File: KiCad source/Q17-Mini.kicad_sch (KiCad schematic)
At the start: 80 parts, among them J1 Input, J2-1 SPK+, J2-2 SPK-, J3-1 V+, J3-2 GND, J3-3 V-, Q1 IRF610, Q10 KSA992, Q11 ZVP2106A, Q12 BD139, Q13 IRF610, Q14 IRF9610, Q15 FQA46N15, Q16 FQA36P15, Q2 KSA992, Q3 KSC1845, Q4 IRF9610, Q5 FQP3P20, Q6 FQP3N30, Q7 KSC1845, Q8 ZVN4206AV, Q9 ZVP2106A, U1 OPA1641

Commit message: Update Q17-Mini.kicad_sch
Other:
- note added: "0.25W, 0.5W resistor : Vishay CCF07 or MRS25"
- note added: "1W resistor : Vishay PR01"
- note added: "2W resistor : Vishay CCF02 or PR02"
- note added: "C13, C14 : Panasonic FC"
- note added: "C3, C5 : ELna Silmic II 100uF 16v"
- note added: "max 55V"
- note removed: "0.5W, 1W resistor : Vishay PR01"
- note removed: "2W resistor : Vishay CCF or PR02"
- note removed: "C3, C5, C13, C14 : Panasonic FC"
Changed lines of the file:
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@@
     (title "Q17-Mini Amplifier")
     (date "2021-12-22")
-    (rev "1.1.7")
+    (rev "1.1.8")
     (company "by eng. Tiberiu Vicol")
     (comment 1 "Modified by Stef for the Q17-Mini project")
@@
     (stroke (width 0) (type solid) (color 0 0 0 0))
   )
-  (text "C3, C5, C13, C14 : Panasonic FC " (at 60.96 170.18 0)
-    (effects (font (size 1.27 1.27)) (justify left bottom))
-  )
-  (text "0.5W, 1W resistor : Vishay PR01" (at 60.96 177.8 0)
+  (text "C3, C5 : ELna Silmic II 100uF 16v" (at 59.69 173.99 0)
+    (effects (font (size 1.27 1.27)) (justify left bottom))
+  )
+  (text "max 55V" (at 266.7 71.12 0)
+    (effects (font (size 1.27 1.27)) (justify left bottom))
+  )
+  (text "1W resistor : Vishay PR01" (at 59.69 177.8 0)
     (effects (font (size 1.27 1.27)) (justify left bottom))
   )
   (text "C1, C10 : use Mica CDE CD15 or Polystyrene capacitor."
-    (at 95.25 193.04 0)
+    (at 96.52 193.04 0)
     (effects (font (size 1.27 1.27)) (justify left bottom))
   )
   (text "J2 and J3: FASTON 250 PCB connector (TE Connectivity 63849-1)"
-    (at 95.25 196.85 0)
+    (at 96.52 196.85 0)
     (effects (font (size 1.27 1.27)) (justify left bottom))
   )
@@
   )
   (text "C7 : use MKP capacitor (MKP1F041005I00JYSD or MKP4D041005D00JSSD)."
-    (at 95.25 181.61 0)
-    (effects (font (size 1.27 1.27)) (justify left bottom))
-  )
-  (text "D2, D3 : 1N5248B" (at 60.96 193.04 0)
-    (effects (font (size 1.27 1.27)) (justify left bottom))
-  )
-  (text "2W resistor : Vishay CCF or PR02" (at 60.96 181.61 0)
+    (at 96.52 181.61 0)
+    (effects (font (size 1.27 1.27)) (justify left bottom))
+  )
+  (text "D2, D3 : 1N5248B" (at 59.69 193.04 0)
+    (effects (font (size 1.27 1.27)) (justify left bottom))
+  )
+  (text "2W resistor : Vishay CCF02 or PR02" (at 59.69 181.61 0)
     (effects (font (size 1.27 1.27)) (justify left bottom))
   )
@@
   )
   (text "R26, R27, R28 : try to use non inductive 1W resistor (Vishay Dale or Ohmite)."
-    (at 95.25 173.99 0)
-    (effects (font (size 1.27 1.27)) (justify left bottom))
-  )
-  (text "D1, D4 : LED RED 2V" (at 60.96 189.23 0)
+    (at 96.52 173.99 0)
+    (effects (font (size 1.27 1.27)) (justify left bottom))
+  )
+  (text "D1, D4 : LED RED 2V" (at 59.69 189.23 0)
     (effects (font (size 1.27 1.27)) (justify left bottom))
   )
@@
   )
   (text "C15, C16 : Vishay 048 RML (MAL204858222E3) or Nichicon UFW (UFW1J222MHD)."
-    (at 95.25 177.8 0)
+    (at 96.52 177.8 0)
     (effects (font (size 1.27 1.27)) (justify left bottom))
   )
@@
   )
   (text "C2 : use bipolar capacitor (Nichicon Muse UES1A101MPM)."
-    (at 95.25 189.23 0)
+    (at 96.52 189.23 0)
+    (effects (font (size 1.27 1.27)) (justify left bottom))
+  )
+  (text "0.25W, 0.5W resistor : Vishay CCF07 or MRS25" (at 96.52 170.18 0)
     (effects (font (size 1.27 1.27)) (justify left bottom))
   )
@@
     (effects (font (size 1.27 1.27)) (justify left bottom))
   )
+  (text "C13, C14 : Panasonic FC " (at 59.69 185.42 0)
+    (effects (font (size 1.27 1.27)) (justify left bottom))
+  )
   (text "Q15 : FQA46N15" (at 13.97 193.04 0)
     (effects (font (size 1.27 1.27)) (justify left bottom))
@@
     (effects (font (size 1.27 1.27)) (justify left bottom))
   )
-  (text "POWER 48VDC" (at 266.7 71.12 0)
+  (text "POWER 48VDC" (at 266.7 68.58 0)
     (effects (font (size 1.27 1.27)) (justify left bottom))
   )
   (text "C17 : use MKP capacitor (MKP1F031004B00KI00 or FKP3C031004C00JSSD)."
-    (at 95.25 185.42 0)
+    (at 96.52 185.42 0)
     (effects (font (size 1.27 1.27)) (justify left bottom))
   )
@@
     (effects (font (size 1.27 1.27)) (justify left bottom))
   )
-  (text "U1 : OPA1641 or OPA1611" (at 60.96 185.42 0)
-    (effects (font (size 1.27 1.27)) (justify left bottom))
-  )
-  (text "D5, D6 : 1N5245" (at 60.96 196.85 0)
-    (effects (font (size 1.27 1.27)) (justify left bottom))
-  )
-  (text "Do not power on the board without opamp." (at 240.03 15.24 0)
-    (effects (font (size 1.27 1.27) (thickness 0.254) bold) (justify left bottom))
-  )
-  (text "100nF capacitor : Wima MKS2" (at 60.96 173.99 0)
-    (effects (font (size 1.27 1.27)) (justify left bottom))
-  )
+  (text "U1 : OPA1641 or OPA1611" (at 13.97 154.94 0)
+    (effects (font (size 1.27 1.27)) (justify left bottom))
+  )
+  (text "D5, D6 : 1N5245" (at 59.69 196.85 0)
+    (effects (font (size 1.27 1.27)) (justify left bottom))
+  )
+  (text "Do not power on the board without opamp." (at 233.68 15.24 0)
+    (effects (font (size 1.5 1.5) (thickness 0.254) bold) (justify left bottom))
+  )
+  (text "100nF capacitor : Wima MKS2" (at 59.69 170.18 0)
+    (effects (font (size 1.27 1.27)) (justify left bottom))
+  )

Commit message: Update diagrams
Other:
- note added: "DC Fuse : 3A Fast"
- note added: "POWER 45VDC"
- note removed: "DC Fuse : 3A"
- note removed: "POWER 48VDC"
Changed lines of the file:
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@@
   (title_block
     (title "Q17-Mini Amplifier")
-    (date "2021-12-22")
+    (date "2021-12-23")
     (rev "1.1.8")
     (company "by eng. Tiberiu Vicol")
@@
     (effects (font (size 1.27 1.27) (thickness 0.254) bold) (justify left bottom))
   )
-  (text "DC Fuse : 3A" (at 266.7 96.52 0)
+  (text "DC Fuse : 3A Fast" (at 264.16 96.52 0)
     (effects (font (size 1.27 1.27)) (justify left bottom))
   )
@@
     (effects (font (size 1.27 1.27)) (justify left bottom))
   )
-  (text "POWER 48VDC" (at 266.7 68.58 0)
-    (effects (font (size 1.27 1.27)) (justify left bottom))
-  )
+  (text "POWER 45VDC" (at 266.7 68.58 0)
+    (effects (font (size 1.27 1.27)) (justify left bottom))
+  )

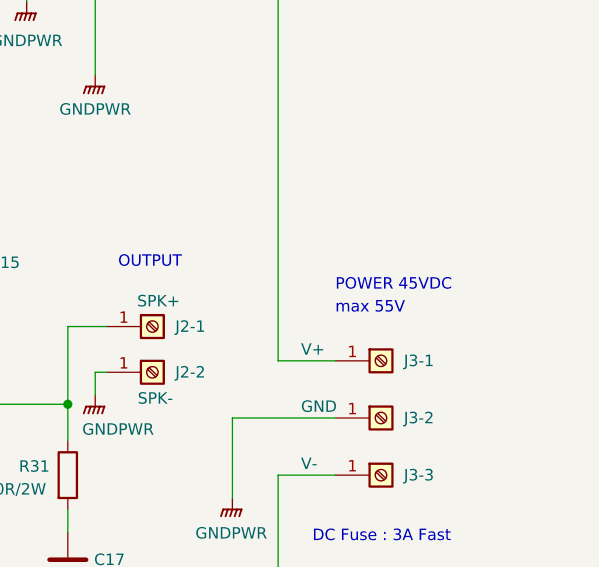
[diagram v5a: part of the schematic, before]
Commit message: Update Q17-Mini diagram
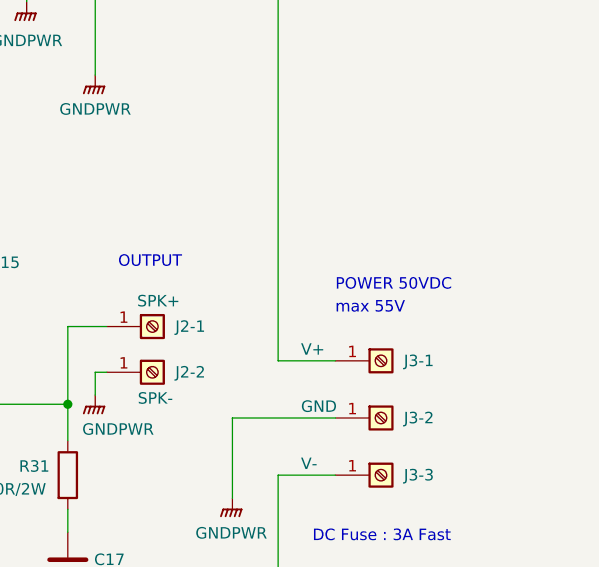
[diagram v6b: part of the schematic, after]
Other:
- note added: "POWER 50VDC"
- note removed: "POWER 45VDC"
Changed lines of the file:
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@@
   (title_block
     (title "Q17-Mini Amplifier")
-    (date "2021-12-23")
-    (rev "1.1.8")
+    (date "2021-12-25")
+    (rev "1.1.9")
     (company "by eng. Tiberiu Vicol")
     (comment 1 "Modified by Stef for the Q17-Mini project")
@@
     (effects (font (size 1.27 1.27)) (justify left bottom))
   )
-  (text "POWER 45VDC" (at 266.7 68.58 0)
-    (effects (font (size 1.27 1.27)) (justify left bottom))
-  )
+  (text "POWER 50VDC" (at 266.7 68.58 0)
+    (effects (font (size 1.27 1.27)) (justify left bottom))
+  )

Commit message: Q17-Mini schematic v1.2.1
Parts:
- R17: value 3k3 -> 7K32
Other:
- note added: "For 0.750v input sensibilkity R17 = 3K3."
- note added: "For input sensibility at 1.5v R17 = 7K32"
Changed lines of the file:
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@@
   (title_block
     (title "Q17-Mini Amplifier")
-    (date "2021-12-25")
-    (rev "1.1.9")
+    (date "2021-12-29")
+    (rev "1.2.1")
     (company "by eng. Tiberiu Vicol")
     (comment 1 "Modified by Stef for the Q17-Mini project")
@@
     (effects (font (size 1.27 1.27)) (justify left bottom))
   )
+  (text "This will give you a coil of 10x20mm (see picture on github repository)."
+    (at 59.69 162.56 0)
+    (effects (font (size 1.27 1.27) (thickness 0.254) bold) (justify left bottom))
+  )
   (text "C7 : use MKP capacitor (MKP1F041005I00JYSD or MKP4D041005D00JSSD)."
     (at 96.52 181.61 0)
@@
     (effects (font (size 1.27 1.27)) (justify left bottom))
   )
+  (text "For input sensibility at 1.5v R17 = 7K32" (at 177.8 160.02 0)
+    (effects (font (size 1.27 1.27)) (justify left bottom))
+  )
   (text "Q5 : FQP3P20" (at 13.97 173.99 0)
     (effects (font (size 1.27 1.27)) (justify left bottom))
   )
+  (text "L1 : 22 turns of a 1mm diameter copper insulated wire wound around a 8mm tube."
+    (at 59.69 158.75 0)
+    (effects (font (size 1.27 1.27) (thickness 0.254) bold) (justify left bottom))
+  )
   (text "OUTPUT" (at 242.57 66.04 0)
     (effects (font (size 1.27 1.27)) (justify left bottom))
-  )
-  (text "L1 : 22 turns of a 1mm diameter copper insulated wire wound around a 8mm tube."
-    (at 60.96 160.02 0)
-    (effects (font (size 1.27 1.27) (thickness 0.254) bold) (justify left bottom))
   )
   (text "DC Fuse : 3A Fast" (at 264.16 96.52 0)
@@
     (effects (font (size 1.27 1.27)) (justify left bottom))
   )
-  (text "This will give you a coil of 10x20mm (see picture on github repository)."
-    (at 60.96 163.83 0)
-    (effects (font (size 1.27 1.27) (thickness 0.254) bold) (justify left bottom))
+  (text "For 0.750v input sensibilkity R17 = 3K3." (at 242.57 165.1 0)
+    (effects (font (size 1.27 1.27)) (justify left bottom))
   )
   (text "Q8 : ZVN4206AV or 2N7000 (not TA)" (at 13.97 181.61 0)
@@
     (in_bom yes) (on_board yes)
     (property "Reference" "R17" (id 0) (at 53.34 91.44 0))
-    (property "Value" "3k3" (id 1) (at 53.34 93.98 0))
+    (property "Value" "7K32" (id 1) (at 53.34 93.98 0))
     (property "Footprint" "Resistor_THT:R_Axial_DIN0207_L6.3mm_D2.5mm_P10.16mm_Horizontal" (id 2) (at 51.308 92.964 90)
       (effects (font (size 1.27 1.27)) hide)
@@
     )
     (path "/7bf364ab-ad4a-477e-ae5d-b48ef62abf83"
-      (reference "R17") (unit 1) (value "3k3") (footprint "Resistor_THT:R_Axial_DIN0207_L6.3mm_D2.5mm_P10.16mm_Horizontal")
+      (reference "R17") (unit 1) (value "7K32") (footprint "Resistor_THT:R_Axial_DIN0207_L6.3mm_D2.5mm_P10.16mm_Horizontal")
     )
     (path "/9ca73c2e-ad4d-444d-ab76-034cbd3e5b45"

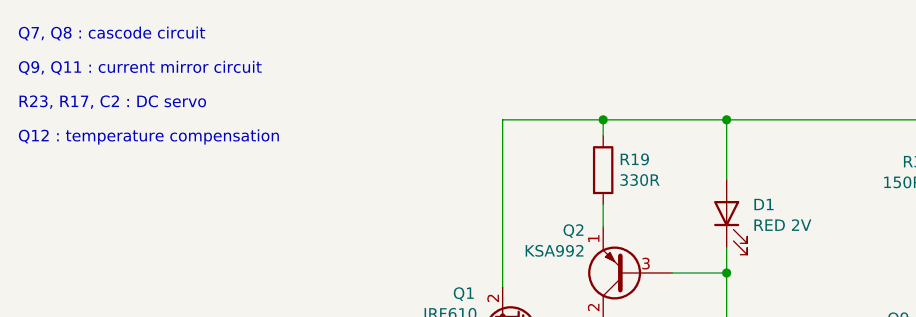
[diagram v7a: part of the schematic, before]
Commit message: Update Q17-Mini-schematic.pdf to 1.2.2
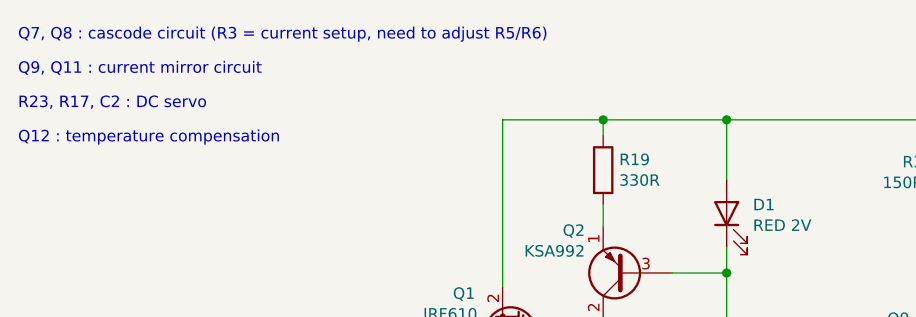
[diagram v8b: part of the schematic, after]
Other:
- note added: "Q7, Q8 : cascode circuit (R3 = current setup, need to adjust R5/R6)"
- note removed: "Q7, Q8 : cascode circuit"
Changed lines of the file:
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@@
   (title_block
     (title "Q17-Mini Amplifier")
-    (date "2021-12-29")
-    (rev "1.2.1")
+    (date "2022-01-02")
+    (rev "1.2.2")
     (company "by eng. Tiberiu Vicol")
     (comment 1 "Modified by Stef for the Q17-Mini project")
@@
     (effects (font (size 1.27 1.27)) (justify left bottom))
   )
-  (text "Q7, Q8 : cascode circuit" (at 13.97 15.24 0)
-    (effects (font (size 1.27 1.27)) (justify left bottom))
-  )
+  (text "Q7, Q8 : cascode circuit (R3 = current setup, need to adjust R5/R6)"
+    (at 13.97 15.24 0)
+    (effects (font (size 1.27 1.27)) (justify left bottom))
+  )
